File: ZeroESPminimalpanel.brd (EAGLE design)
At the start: 50.8 x 22.9 mm, 38 parts, among them IC1 MCP1703DB, IC2 MCP1703DB, X1 BU-SMA-G, X2 BU-SMA-G

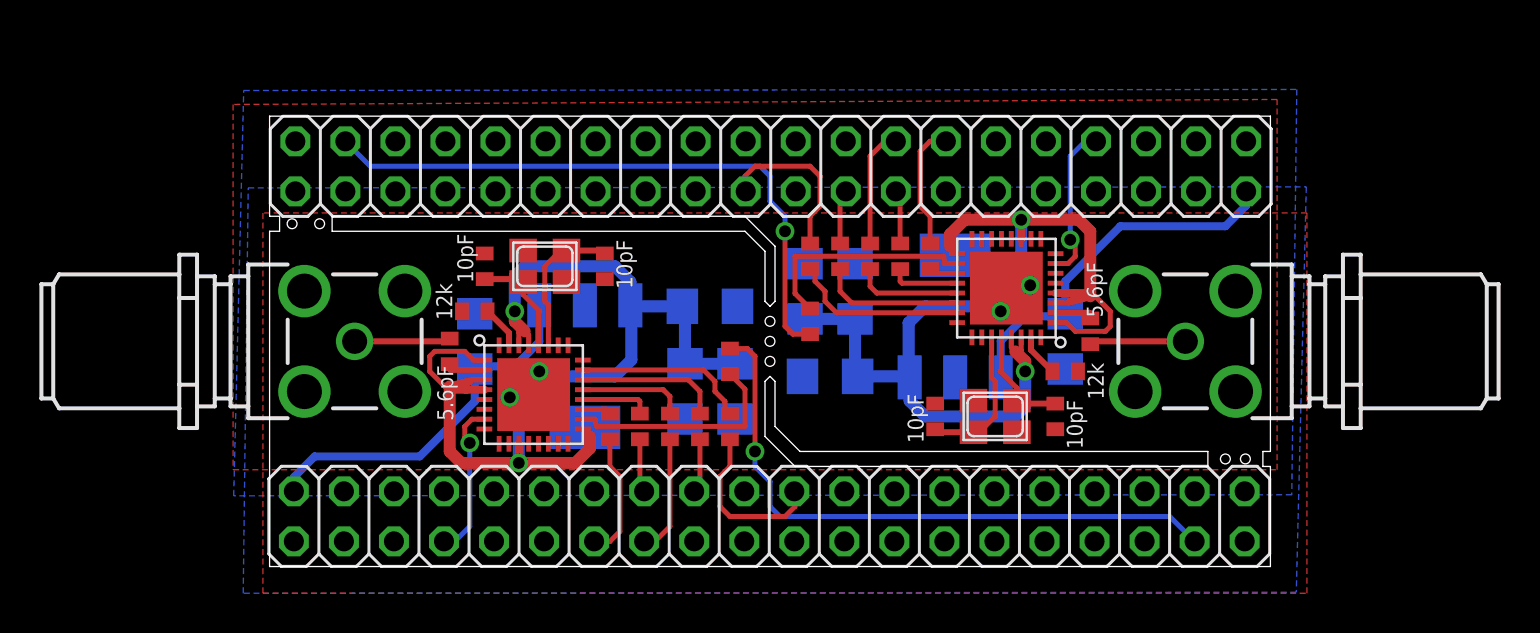
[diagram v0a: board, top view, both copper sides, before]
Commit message: connected ground pad of leo
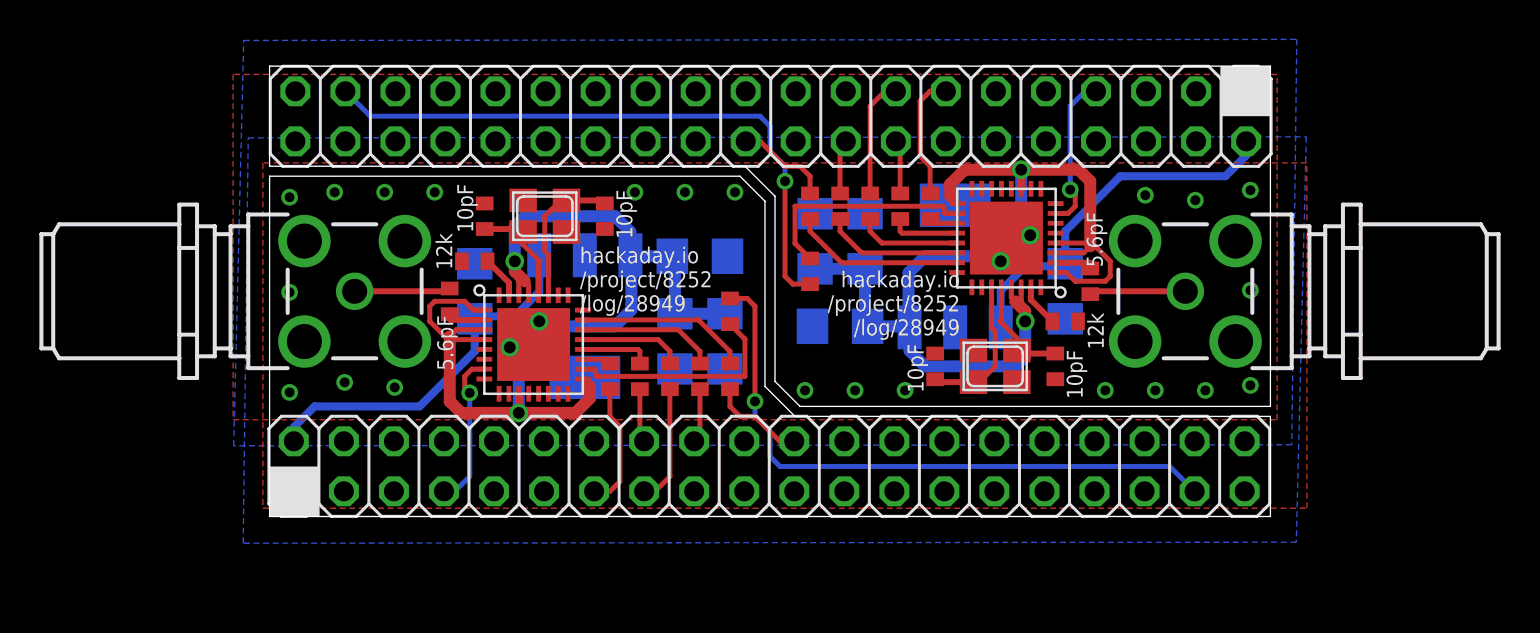
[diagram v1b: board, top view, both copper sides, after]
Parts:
- moved C10 2.59 mm to (27.7, 16.5)
- moved C11 2.59 mm to (29.0, 12.2)
- moved C9 2.59 mm to (30.2, 16.5)
- moved C2 2.59 mm to (20.6, 11.4)
- moved C3 2.59 mm to (23.1, 11.4)
- moved C4 2.59 mm to (21.8, 15.7)
- moved C1 2.54 mm to (10.4, 14.0)
- moved C6 2.54 mm to (17.0, 17.8)
- moved C7 2.54 mm to (10.9, 17.8)
- moved C8 2.54 mm to (40.4, 14.0)
- moved IC1 2.54 mm to (34.8, 15.2)
- moved Q1 2.54 mm to (14.0, 17.8)
- moved R1 2.54 mm to (23.4, 13.0)
- moved R10 2.54 mm to (33.5, 18.3)
- moved R11 2.54 mm to (32.0, 18.3)
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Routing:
- net SD_D5: track 8.64 -> 4.97 mm
- net SD_D1: track 8.64 -> 4.97 mm
- net VCC1: track 55.4 -> 54.1 mm
- net VCC3: track 55.4 -> 54.1 mm
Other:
- outline, holes or cut-outs redrawn
- board text added: "hackaday.io /project/8252 /log/28949"
- board text added: "hackaday.io/davedarko"
